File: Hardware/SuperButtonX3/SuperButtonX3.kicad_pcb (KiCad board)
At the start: 2 copper layers, 53.2 x 53.2 mm, 25 parts, among them J101 USBC, J103 EXT_LED, SW101 Switch, SW102 PROG, U101 CH552G

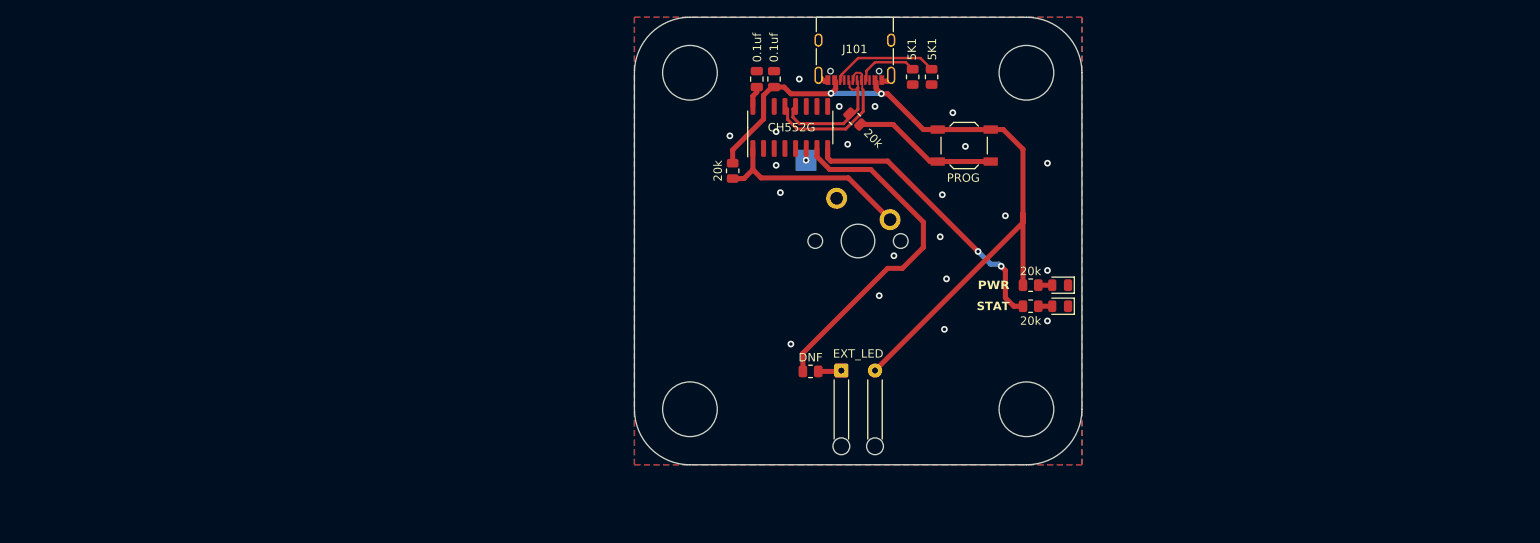
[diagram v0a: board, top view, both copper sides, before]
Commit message: increased width of board, moved a couple of the components around to help better fit the wiring for the two new buttons, not finished yet.
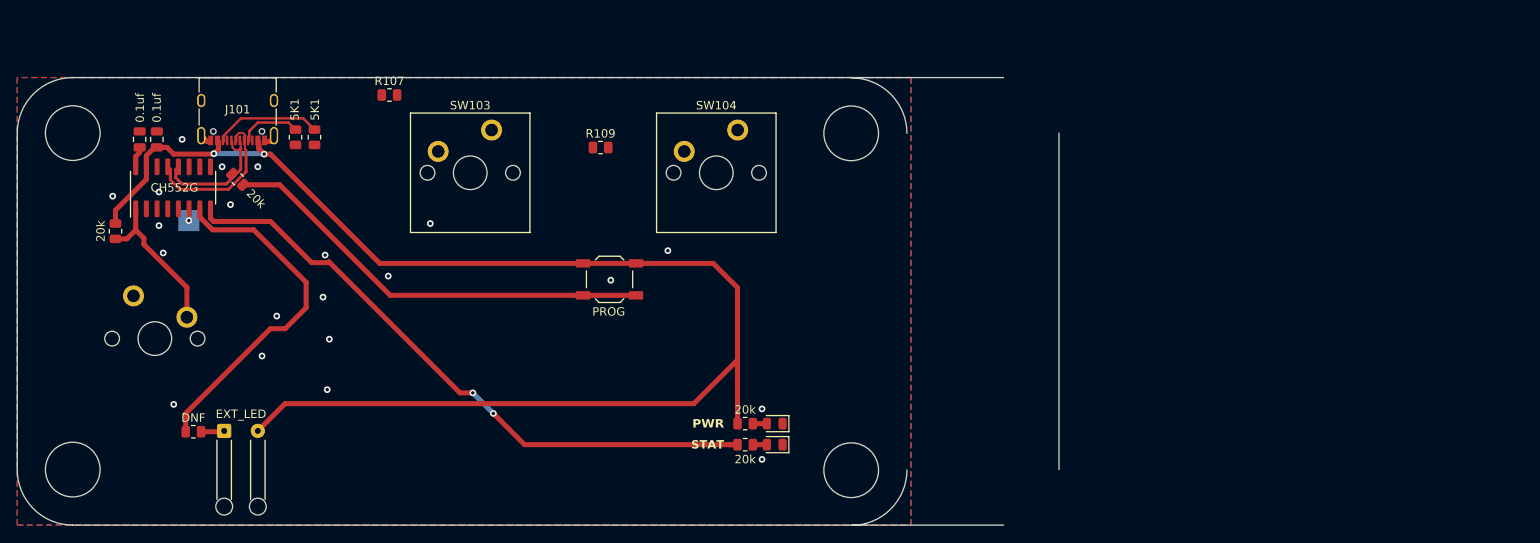
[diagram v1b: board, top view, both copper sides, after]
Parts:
- added R107: 20k, Resistor_SMD:R_0805_2012Metric, F.Cu at (116.3, 72.6)
- added R109: 20k, Resistor_SMD:R_0805_2012Metric, F.Cu at (141.4, 78.9)
- added SW103: Switch, Switch_Keyboard_Cherry_MX:SW_Cherry_MX_PCB, F.Cu at (125.9, 81.9)
- added SW104: Switch, Switch_Keyboard_Cherry_MX:SW_Cherry_MX_PCB, F.Cu at (155.1, 81.9)
- moved SW101 84.4 mm to (88.4, 101.6)
- moved R101 73.7 mm to (107.4, 77.7)
- moved R102 73.7 mm to (105.1, 77.7)
- moved R105 73.7 mm to (83.7, 88.8)
- moved R108 73.7 mm to (93.0, 112.7)
- moved REF** 73.7 mm to (80.4, 100.0)
- moved REF** 73.7 mm to (80.1, 90.4)
- moved TP101 73.7 mm to (92.4, 87.6)
- moved U101 73.7 mm to (90.6, 83.7)
- moved C104 73.7 mm to (88.6, 77.9)
- moved H102 73.7 mm to (78.6, 117.2)
- moved H103 73.7 mm to (78.6, 77.2)
- moved J101 73.7 mm to (98.2, 74.4)
- moved J103 73.7 mm to (96.6, 112.6)
- moved C101 73.7 mm to (86.6, 77.9)
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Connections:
- net /SW_SENSE renamed /SW_SENSE1
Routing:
- net +5V: track 90.7 -> 170.0 mm
- net /STAT: track 33.5 -> 76.1 mm
- net Net-(R104-Pad1): track 17.3 -> 53.9 mm
- net /SW_SENSE1: track 24.1 -> 18.2 mm
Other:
- board size 53.2 x 53.2 mm -> 123.8 x 53.2 mm

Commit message: Clean up x3 board
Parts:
- SW103, SW104: moved to B.Cu
- moved TP101 124.9 mm to (217.1, 80.0)
- moved U101 124.9 mm to (215.2, 76.1)
- moved C104 124.9 mm to (213.3, 70.3)
- moved C101 124.9 mm to (211.3, 70.3)
- moved R104 124.9 mm to (222.9, 75.1)
- moved R105 124.9 mm to (208.4, 81.3)
- moved J101 124.8 mm to (222.9, 67.3)
- moved R101 124.8 mm to (232.0, 70.6)
- moved R102 124.8 mm to (229.8, 70.6)
- moved J103 118.4 mm to (214.8, 105.8)
- moved R108 118.4 mm to (211.1, 105.9)
- moved R107 112.3 mm to (228.0, 83.8), turned to -135 degrees
- moved SW102 91.7 mm to (232.2, 76.0)
- moved D103 87.5 mm to (248.9, 102.9)
- moved D104 87.5 mm to (248.9, 100.4)
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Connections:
- U101 pad 10: unconnected-(U101-P3.3-Pad10) -> /SW_SENSE2
- U101 pad 11: unconnected-(U101-P3.4-Pad11) -> /SW_SENSE3
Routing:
- net +5V: track 170.0 -> 0.00 mm, vias 2 -> 0
- net /STAT: track 76.1 -> 0.00 mm, vias 2 -> 0
- net Net-(R104-Pad1): track 53.9 -> 0.00 mm
- net /EXT: track 41.6 -> 0.00 mm
- net /USB-: track 18.4 -> 0.00 mm
- net /SW_SENSE1: track 18.2 -> 0.00 mm
- net /USB+: track 15.8 -> 0.00 mm
- net Net-(J101-CC2): track 12.9 -> 0.00 mm
- net Net-(J101-CC1): track 7.50 -> 0.00 mm
- net Net-(J103-Pin_1): track 2.79 -> 0.00 mm
- net +3V3: track 2.49 -> 0.00 mm
- net GND: track 2.41 -> 0.00 mm, vias 21 -> 0
- net Net-(D104-A): track 1.66 -> 0.00 mm
- net Net-(D103-A): track 1.66 -> 0.00 mm
- net /RST: track 1.41 -> 0.00 mm, vias 1 -> 0
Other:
- board size 123.8 x 53.2 mm -> 105.6 x 53.2 mm

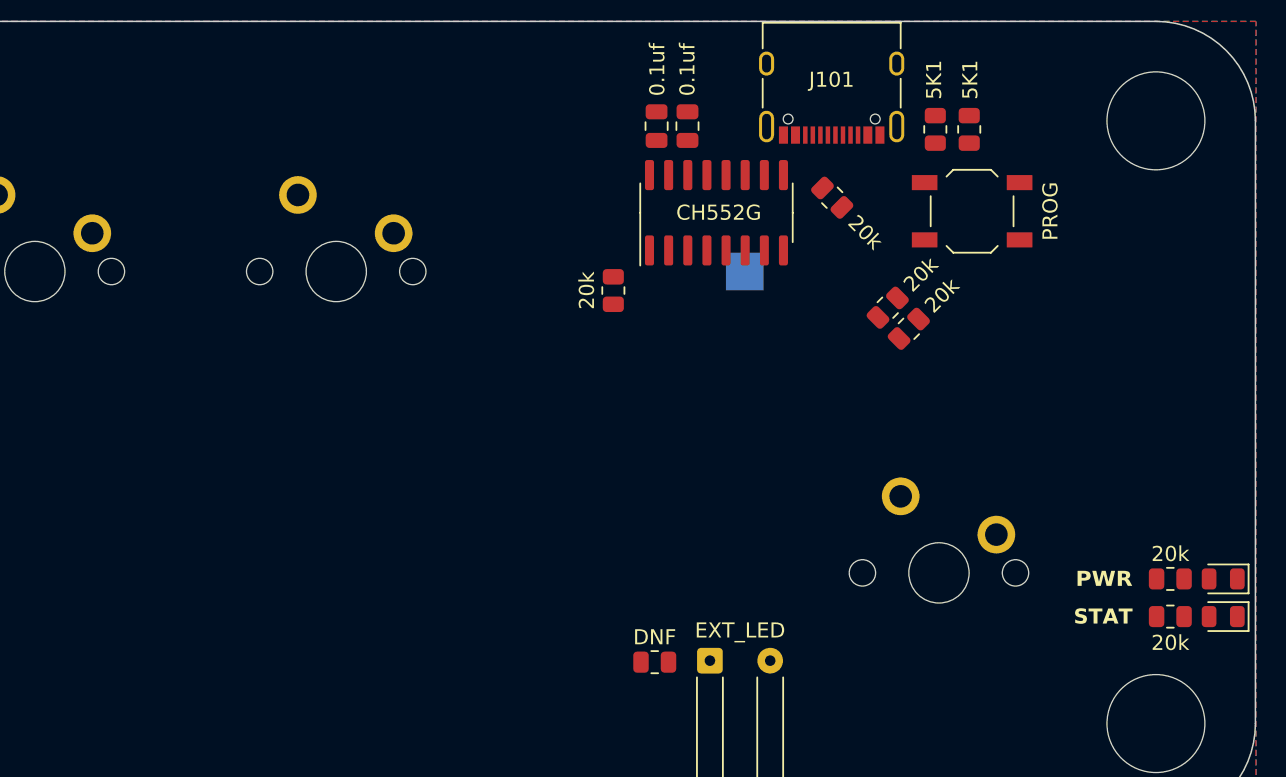
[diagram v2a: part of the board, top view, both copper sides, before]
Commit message: I don't like how this is routed, but I thought I'd leave it at this for now, I would like to move a couple of things around for the sake of easier routing
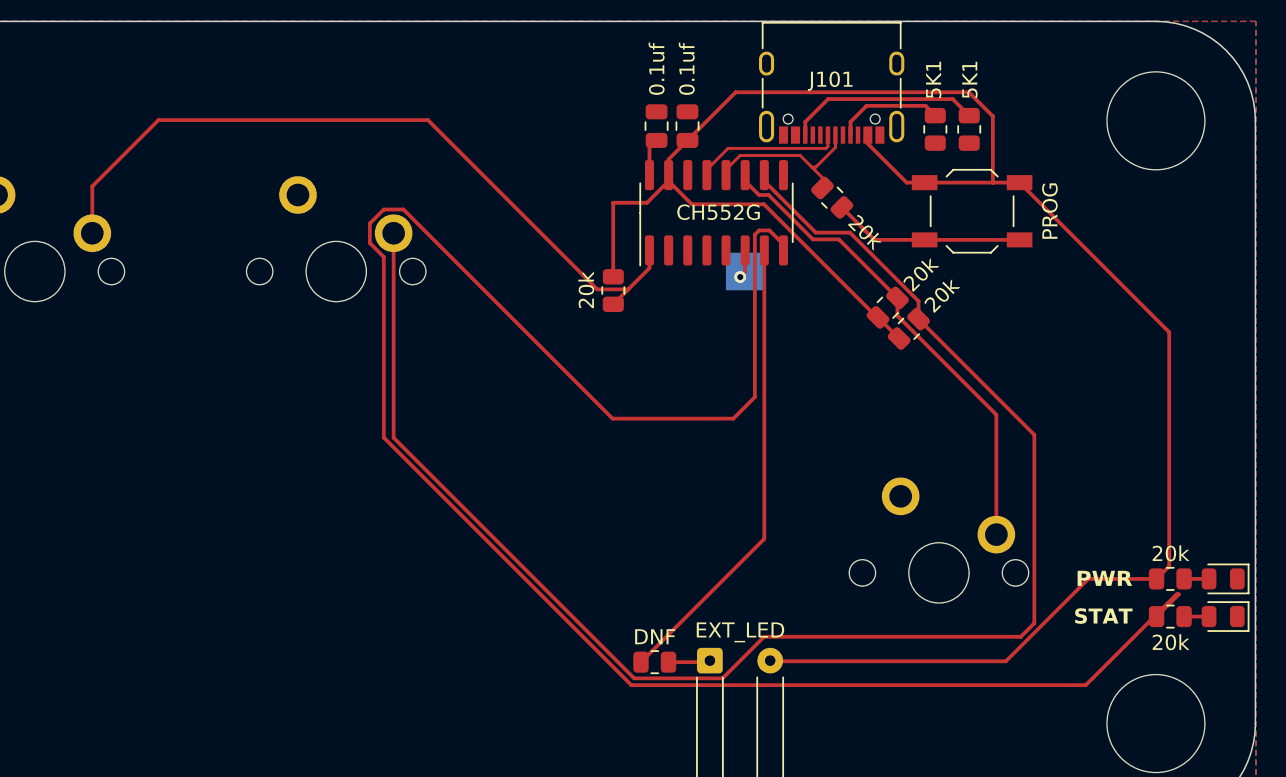
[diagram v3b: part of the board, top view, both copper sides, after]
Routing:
- net +5V: track 0.00 -> 129.1 mm
- net /STAT: track 0.00 -> 124.6 mm
- net /SW_SENSE2: track 0.00 -> 102.7 mm
- net /SW_SENSE1: track 0.00 -> 49.8 mm
- net /SW_SENSE3: track 0.00 -> 32.1 mm
- net /EXT: track 0.00 -> 30.7 mm
- net Net-(J101-CC2): track 0.00 -> 12.8 mm
- net Net-(R104-Pad1): track 0.00 -> 12.7 mm
- net /USB+: track 0.00 -> 11.4 mm
- net /USB-: track 0.00 -> 9.79 mm
- net Net-(J101-CC1): track 0.00 -> 7.21 mm
- net Net-(J103-Pin_1): track 0.00 -> 2.79 mm
- net +3V3: track 0.00 -> 2.49 mm
- net /RST: track 0.00 -> 2.39 mm, vias 0 -> 1
- net Net-(D104-A): track 0.00 -> 1.66 mm
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
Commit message: Fix routing
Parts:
- moved R107 18.7 mm to (209.4, 82.4), turned to -90 degrees
- moved R109 15.2 mm to (211.4, 82.4), turned to -90 degrees
- moved C101 2.67 mm to (208.6, 70.5)
- moved C104 2.52 mm to (210.8, 70.5)
- moved TP101 2.22 mm to (214.9, 80.2)
- moved U101 2.22 mm to (213.0, 76.3)
- moved R104 1.60 mm to (221.4, 74.6)
- moved R105 1.51 mm to (207.4, 82.4), turned to -90 degrees
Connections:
- U101 pad 10: /SW_SENSE2 -> unconnected-(U101-P3.3-Pad10)
- U101 pad 11: /SW_SENSE3 -> unconnected-(U101-P3.4-Pad11)
- U101 pad 2: unconnected-(U101-P1.4-Pad2) -> /SW_SENSE2
- U101 pad 3: unconnected-(U101-P1.5-Pad3) -> /SW_SENSE3
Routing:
- net /STAT: track 124.6 -> 37.9 mm
- net /SW_SENSE2: track 102.7 -> 20.2 mm, vias 0 -> 1
- net +5V: track 129.1 -> 100.3 mm, vias 0 -> 7
- net /SW_SENSE1: track 49.8 -> 39.7 mm, vias 0 -> 1
- net /USB-: track 9.79 -> 17.4 mm
- net /USB+: track 11.4 -> 16.7 mm
- net GND: track 0.00 -> 3.01 mm, vias 0 -> 17
- net Net-(R104-Pad1): track 12.7 -> 14.4 mm
- net /EXT: track 30.7 -> 29.6 mm
- net /RST: track 2.39 -> 1.41 mm
- net Net-(J101-CC2): track 12.8 -> 13.7 mm
- net Net-(J101-CC1): track 7.21 -> 7.86 mm
- net /SW_SENSE3: track 32.1 -> 31.8 mm, vias 0 -> 1
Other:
- board text added: "3X Buttton By FRC 1721 Tidal Force https://www.frc1721.org/ ${FULL_REVISION}"
- board text added: "C"
- board text added: "CTRL"
- board text added: "Design by Jack Sophmore Asst. Lead of Software"
- board text added: "V"
- board text removed: "Super Buttton By FRC 1721 Tidal Force https://www.frc1721.org/ ${FULL_REVISION}"

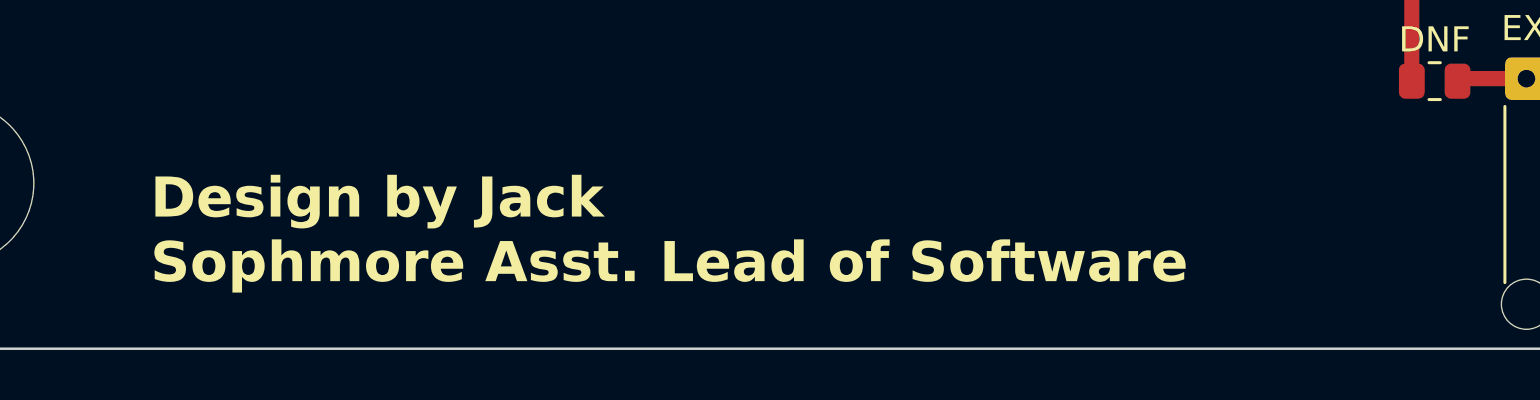
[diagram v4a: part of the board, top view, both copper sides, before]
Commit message: Fix Jack's name
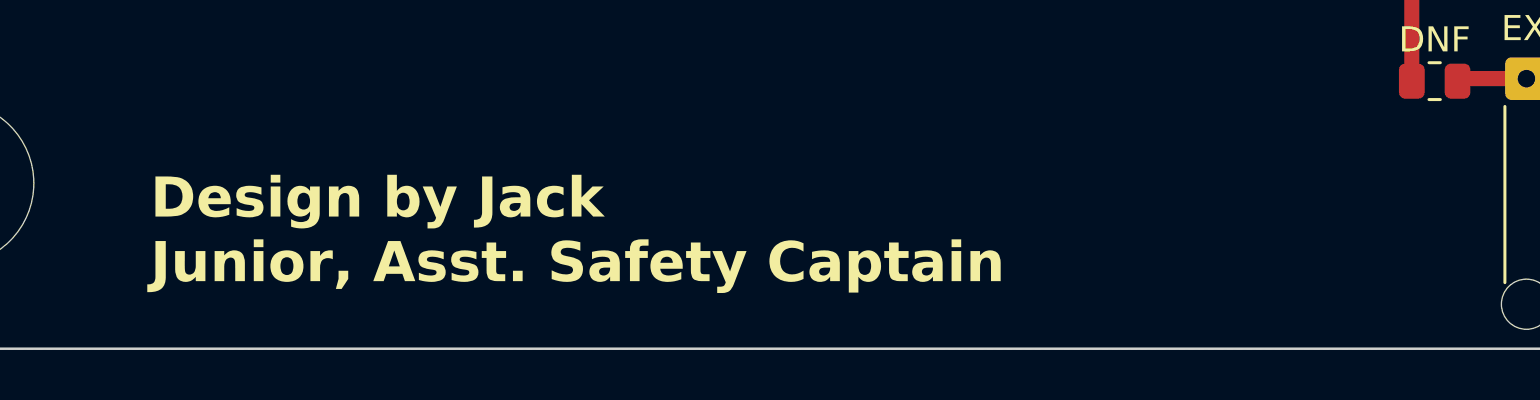
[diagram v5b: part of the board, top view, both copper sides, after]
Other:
- board text added: "Design by Jack Junior, Asst. Safety Captain"
- board text removed: "Design by Jack Sophmore Asst. Lead of Software"
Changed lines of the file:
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@@
     (effects (font (size 1.6 1.6) (thickness 0.4) bold) (justify mirror))
   )
-  (gr_text "Design by Jack\nSophmore Asst. Lead of Software" (at 159.9 114.1) (layer "F.SilkS")
+  (gr_text "Design by Jack\nJunior, Asst. Safety Captain " (at 159.9 114.1) (layer "F.SilkS")
     (effects (font (size 1.6 1.6) (thickness 0.4) bold) (justify left bottom))
   )

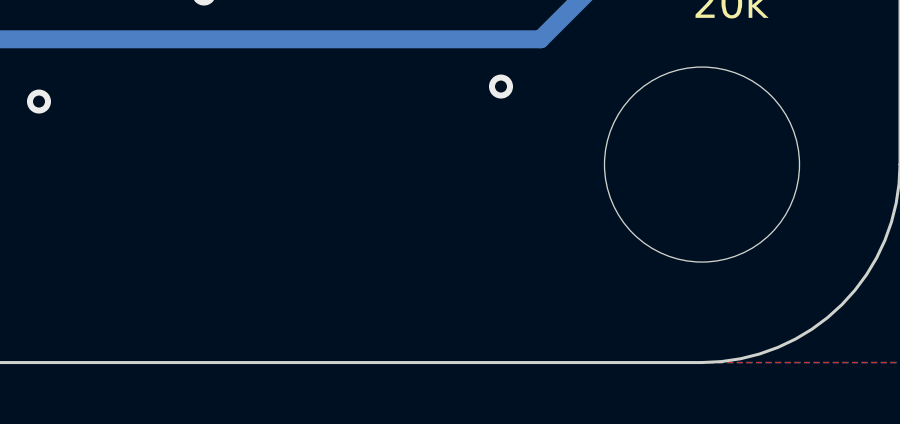
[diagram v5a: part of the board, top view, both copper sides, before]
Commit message: Add JLCJLCJLC to boards
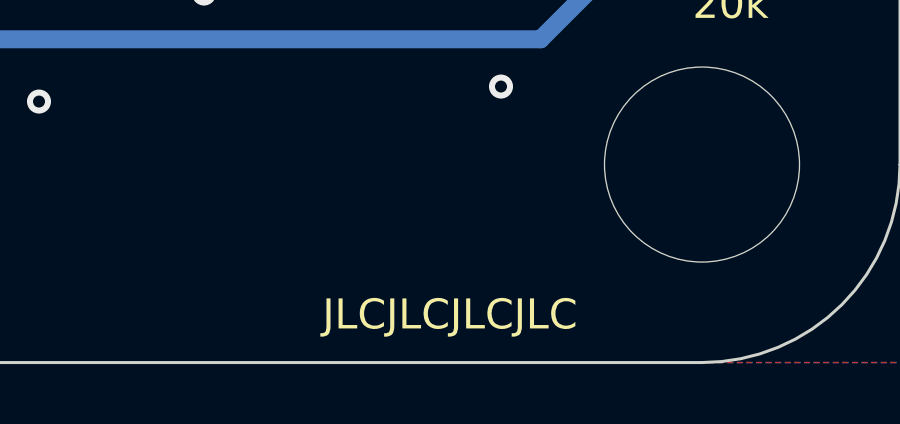
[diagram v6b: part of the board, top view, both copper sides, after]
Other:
- board text added: "JLCJLCJLCJLC"
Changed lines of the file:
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@@
     (effects (font (size 1.6 1.6) (thickness 0.4) bold) (justify mirror))
+  )
+  (gr_text "JLCJLCJLCJLC" (at 236 115) (layer "F.SilkS")
+    (effects (font (size 1 1) (thickness 0.25)))
   )
   (gr_text "Design by Jack\nJunior, Asst. Safety Captain " (at 159.9 114.1) (layer "F.SilkS")
